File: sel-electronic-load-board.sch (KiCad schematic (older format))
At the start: 44 parts, among them J1 HE10 receptacle, Q1 N-mosfet, Q10 N-mosfet, Q11 N-mosfet, Q12 N-mosfet, Q13 N-mosfet, Q14 N-mosfet, Q15 N-mosfet, Q16 N-mosfet, Q2 N-mosfet, Q3 N-mosfet, Q4 N-mosfet, Q5 N-mosfet, Q6 N-mosfet, Q7 N-mosfet, Q8 N-mosfet, Q9 N-mosfet, SW1 DMM bypass, U1 OpAmp, U2 Input stage, U3 Output stage, U4 Current sensor

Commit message: assigning footprint, missing lever switch
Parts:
- F1: footprint (none) -> Fuse:Fuseholder_Cylinder-5x20mm_Stelvio-Kontek_PTF78_Horizontal_Open
- H1, H2, H3, H4: footprint (none) -> MountingHole:MountingHole_4.3mm_M4_Pad
- H5, H6, H7, H8: footprint (none) -> MountingHole:MountingHole_4.3mm_M4
- J1: footprint (none) -> Connector_IDC:IDC-Header_2x05_P2.54mm_Horizontal
- JP1: footprint (none) -> Jumper:SolderJumper-2_P1.3mm_Open_RoundedPad1.0x1.5mm
- Q1, Q10, Q11, Q12, Q13, Q14, Q15, Q16, Q2, Q3, Q4, Q5, Q6, Q7, Q8, Q9: footprint electronic-load:TO220-GDS-Heatsink-1000mils-interaxe-91mils-pin-radius -> Package_TO_SOT_THT:TO-220-3_Vertical
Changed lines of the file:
@@
 F 0 "Q1" H 1400 1550 50  0000 L CNN
 F 1 "N-mosfet" H 1400 1450 50  0000 L CNN
-F 2 "electronic-load:TO220-GDS-Heatsink-1000mils-interaxe-91mils-pin-radius" H 1400 1600 50  0001 C CNN
+F 2 "Package_TO_SOT_THT:TO-220-3_Vertical" H 1400 1600 50  0001 C CNN
 F 3 "~" H 1200 1500 50  0001 C CNN
 	1    1200 1500
@@
 F 0 "Q2" H 2600 1550 50  0000 L CNN
 F 1 "N-mosfet" H 2600 1450 50  0000 L CNN
-F 2 "electronic-load:TO220-GDS-Heatsink-1000mils-interaxe-91mils-pin-radius" H 2600 1600 50  0001 C CNN
+F 2 "Package_TO_SOT_THT:TO-220-3_Vertical" H 2600 1600 50  0001 C CNN
 F 3 "~" H 2400 1500 50  0001 C CNN
 	1    2400 1500
@@
 F 0 "Q3" H 3800 1550 50  0000 L CNN
 F 1 "N-mosfet" H 3800 1450 50  0000 L CNN
-F 2 "electronic-load:TO220-GDS-Heatsink-1000mils-interaxe-91mils-pin-radius" H 3800 1600 50  0001 C CNN
+F 2 "Package_TO_SOT_THT:TO-220-3_Vertical" H 3800 1600 50  0001 C CNN
 F 3 "~" H 3600 1500 50  0001 C CNN
 	1    3600 1500
@@
 F 0 "Q4" H 5000 1550 50  0000 L CNN
 F 1 "N-mosfet" H 5000 1450 50  0000 L CNN
-F 2 "electronic-load:TO220-GDS-Heatsink-1000mils-interaxe-91mils-pin-radius" H 5000 1600 50  0001 C CNN
+F 2 "Package_TO_SOT_THT:TO-220-3_Vertical" H 5000 1600 50  0001 C CNN
 F 3 "~" H 4800 1500 50  0001 C CNN
 	1    4800 1500
@@
 F 0 "Q5" H 1400 2550 50  0000 L CNN
 F 1 "N-mosfet" H 1400 2450 50  0000 L CNN
-F 2 "electronic-load:TO220-GDS-Heatsink-1000mils-interaxe-91mils-pin-radius" H 1400 2600 50  0001 C CNN
+F 2 "Package_TO_SOT_THT:TO-220-3_Vertical" H 1400 2600 50  0001 C CNN
 F 3 "~" H 1200 2500 50  0001 C CNN
 	1    1200 2500
@@
 F 0 "Q6" H 2600 2550 50  0000 L CNN
 F 1 "N-mosfet" H 2600 2450 50  0000 L CNN
-F 2 "electronic-load:TO220-GDS-Heatsink-1000mils-interaxe-91mils-pin-radius" H 2600 2600 50  0001 C CNN
+F 2 "Package_TO_SOT_THT:TO-220-3_Vertical" H 2600 2600 50  0001 C CNN
 F 3 "~" H 2400 2500 50  0001 C CNN
 	1    2400 2500
@@
 F 0 "Q7" H 3800 2550 50  0000 L CNN
 F 1 "N-mosfet" H 3800 2450 50  0000 L CNN
-F 2 "electronic-load:TO220-GDS-Heatsink-1000mils-interaxe-91mils-pin-radius" H 3800 2600 50  0001 C CNN
+F 2 "Package_TO_SOT_THT:TO-220-3_Vertical" H 3800 2600 50  0001 C CNN
 F 3 "~" H 3600 2500 50  0001 C CNN
 	1    3600 2500
@@
 F 0 "Q8" H 5000 2550 50  0000 L CNN
 F 1 "N-mosfet" H 5000 2450 50  0000 L CNN
-F 2 "electronic-load:TO220-GDS-Heatsink-1000mils-interaxe-91mils-pin-radius" H 5000 2600 50  0001 C CNN
+F 2 "Package_TO_SOT_THT:TO-220-3_Vertical" H 5000 2600 50  0001 C CNN
 F 3 "~" H 4800 2500 50  0001 C CNN
 	1    4800 2500
@@
 F 0 "Q9" H 1400 3550 50  0000 L CNN
 F 1 "N-mosfet" H 1400 3450 50  0000 L CNN
-F 2 "electronic-load:TO220-GDS-Heatsink-1000mils-interaxe-91mils-pin-radius" H 1400 3600 50  0001 C CNN
+F 2 "Package_TO_SOT_THT:TO-220-3_Vertical" H 1400 3600 50  0001 C CNN
 F 3 "~" H 1200 3500 50  0001 C CNN
 	1    1200 3500
@@
 F 0 "Q10" H 2600 3550 50  0000 L CNN
 F 1 "N-mosfet" H 2600 3450 50  0000 L CNN
-F 2 "electronic-load:TO220-GDS-Heatsink-1000mils-interaxe-91mils-pin-radius" H 2600 3600 50  0001 C CNN
+F 2 "Package_TO_SOT_THT:TO-220-3_Vertical" H 2600 3600 50  0001 C CNN
 F 3 "~" H 2400 3500 50  0001 C CNN
 	1    2400 3500
@@
 F 0 "Q11" H 3800 3550 50  0000 L CNN
 F 1 "N-mosfet" H 3800 3450 50  0000 L CNN
-F 2 "electronic-load:TO220-GDS-Heatsink-1000mils-interaxe-91mils-pin-radius" H 3800 3600 50  0001 C CNN
+F 2 "Package_TO_SOT_THT:TO-220-3_Vertical" H 3800 3600 50  0001 C CNN
 F 3 "~" H 3600 3500 50  0001 C CNN
 	1    3600 3500
@@
 F 0 "Q12" H 5000 3550 50  0000 L CNN
 F 1 "N-mosfet" H 5000 3450 50  0000 L CNN
-F 2 "electronic-load:TO220-GDS-Heatsink-1000mils-interaxe-91mils-pin-radius" H 5000 3600 50  0001 C CNN
+F 2 "Package_TO_SOT_THT:TO-220-3_Vertical" H 5000 3600 50  0001 C CNN
 F 3 "~" H 4800 3500 50  0001 C CNN
 	1    4800 3500
@@
 F 0 "Q13" H 1400 4550 50  0000 L CNN
 F 1 "N-mosfet" H 1400 4450 50  0000 L CNN
-F 2 "electronic-load:TO220-GDS-Heatsink-1000mils-interaxe-91mils-pin-radius" H 1400 4600 50  0001 C CNN
+F 2 "Package_TO_SOT_THT:TO-220-3_Vertical" H 1400 4600 50  0001 C CNN
 F 3 "~" H 1200 4500 50  0001 C CNN
 	1    1200 4500
@@
 F 0 "Q14" H 2600 4550 50  0000 L CNN
 F 1 "N-mosfet" H 2600 4450 50  0000 L CNN
-F 2 "electronic-load:TO220-GDS-Heatsink-1000mils-interaxe-91mils-pin-radius" H 2600 4600 50  0001 C CNN
+F 2 "Package_TO_SOT_THT:TO-220-3_Vertical" H 2600 4600 50  0001 C CNN
 F 3 "~" H 2400 4500 50  0001 C CNN
 	1    2400 4500
@@
 F 0 "Q15" H 3800 4550 50  0000 L CNN
 F 1 "N-mosfet" H 3800 4450 50  0000 L CNN
-F 2 "electronic-load:TO220-GDS-Heatsink-1000mils-interaxe-91mils-pin-radius" H 3800 4600 50  0001 C CNN
+F 2 "Package_TO_SOT_THT:TO-220-3_Vertical" H 3800 4600 50  0001 C CNN
 F 3 "~" H 3600 4500 50  0001 C CNN
 	1    3600 4500
@@
 F 0 "Q16" H 5000 4550 50  0000 L CNN
 F 1 "N-mosfet" H 5000 4450 50  0000 L CNN
-F 2 "electronic-load:TO220-GDS-Heatsink-1000mils-interaxe-91mils-pin-radius" H 5000 4600 50  0001 C CNN
+F 2 "Package_TO_SOT_THT:TO-220-3_Vertical" H 5000 4600 50  0001 C CNN
 F 3 "~" H 4800 4500 50  0001 C CNN
 	1    4800 4500
@@
 F 0 "H2" H 3100 6350 50  0000 C CNN
 F 1 "DUT-" H 3100 6275 50  0000 C CNN
-F 2 "" H 3100 6100 50  0001 C CNN
+F 2 "MountingHole:MountingHole_4.3mm_M4_Pad" H 3100 6100 50  0001 C CNN
 F 3 "~" H 3100 6100 50  0001 C CNN
 	1    3100 6100
@@
 F 0 "H4" H 3850 6350 50  0000 C CNN
 F 1 "DMM-" H 3850 6275 50  0000 C CNN
-F 2 "" H 3850 6100 50  0001 C CNN
+F 2 "MountingHole:MountingHole_4.3mm_M4_Pad" H 3850 6100 50  0001 C CNN
 F 3 "~" H 3850 6100 50  0001 C CNN
 	1    3850 6100
@@
 F 0 "H3" H 3600 6350 50  0000 C CNN
 F 1 "DMM+" H 3600 6275 50  0000 C CNN
-F 2 "" H 3600 6100 50  0001 C CNN
+F 2 "MountingHole:MountingHole_4.3mm_M4_Pad" H 3600 6100 50  0001 C CNN
 F 3 "~" H 3600 6100 50  0001 C CNN
 	1    3600 6100
@@
 F 0 "H1" H 2850 6350 50  0000 C CNN
 F 1 "DUT+" H 2850 6275 50  0000 C CNN
-F 2 "" H 2850 6100 50  0001 C CNN
+F 2 "MountingHole:MountingHole_4.3mm_M4_Pad" H 2850 6100 50  0001 C CNN
 F 3 "~" H 2850 6100 50  0001 C CNN
 	1    2850 6100
@@
 F 0 "F1" V 3430 6500 50  0000 C CNN
 F 1 "Fuse 4A" V 3275 6500 50  0000 C CNN
-F 2 "" V 3280 6500 50  0001 C CNN
+F 2 "Fuse:Fuseholder_Cylinder-5x20mm_Stelvio-Kontek_PTF78_Horizontal_Open" V 3280 6500 50  0001 C CNN
 F 3 "~" H 3350 6500 50  0001 C CNN
 	1    3350 6500
@@
 F 0 "J1" H 1500 6600 50  0000 C CNN
 F 1 "HE10 receptacle" H 1500 6000 50  0000 C CNN
-F 2 "" H 1450 6300 50  0001 C CNN
+F 2 "Connector_IDC:IDC-Header_2x05_P2.54mm_Horizontal" H 1450 6300 50  0001 C CNN
 F 3 "~" H 1450 6300 50  0001 C CNN
 	1    1450 6300
@@
 F 0 "H5" H 6500 6700 50  0000 C CNN
 F 1 "MountingHole" H 6500 6625 50  0000 C CNN
-F 2 "" H 6500 6500 50  0001 C CNN
+F 2 "MountingHole:MountingHole_4.3mm_M4" H 6500 6500 50  0001 C CNN
 F 3 "~" H 6500 6500 50  0001 C CNN
 	1    6500 6500
@@
 F 0 "H6" H 6500 7050 50  0000 C CNN
 F 1 "MountingHole" H 6500 6975 50  0000 C CNN
-F 2 "" H 6500 6850 50  0001 C CNN
+F 2 "MountingHole:MountingHole_4.3mm_M4" H 6500 6850 50  0001 C CNN
 F 3 "~" H 6500 6850 50  0001 C CNN
 	1    6500 6850
@@
 F 0 "H7" H 6500 7400 50  0000 C CNN
 F 1 "MountingHole" H 6500 7325 50  0000 C CNN
-F 2 "" H 6500 7200 50  0001 C CNN
+F 2 "MountingHole:MountingHole_4.3mm_M4" H 6500 7200 50  0001 C CNN
 F 3 "~" H 6500 7200 50  0001 C CNN
 	1    6500 7200
@@
 F 0 "H8" H 6500 7750 50  0000 C CNN
 F 1 "MountingHole" H 6500 7675 50  0000 C CNN
-F 2 "" H 6500 7550 50  0001 C CNN
+F 2 "MountingHole:MountingHole_4.3mm_M4" H 6500 7550 50  0001 C CNN
 F 3 "~" H 6500 7550 50  0001 C CNN
 	1    6500 7550
@@
 F 0 "JP1" H 5250 7180 50  0000 C CNN
 F 1 "If needed by the IC" H 5250 6950 50  0000 C CNN
-F 2 "" H 5250 7100 50  0001 C CNN
+F 2 "Jumper:SolderJumper-2_P1.3mm_Open_RoundedPad1.0x1.5mm" H 5250 7100 50  0001 C CNN
 F 3 "~" H 5250 7100 50  0001 C CNN
 	1    5250 7100

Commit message: update metadata, use custom footprint for toggle switch
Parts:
- SW1: footprint (none) -> switches:toggle-switch-P4.70mm-3pins-75mils-vias
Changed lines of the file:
@@
 encoding utf-8
 Sheet 1 1
-Title ""
-Date "2022-05-13"
-Rev ""
+Title "Electronic load module"
+Date "2022-05-15"
+Rev "1.0.0-draft"
 Comp ""
 Comment1 ""
@@
 F 0 "SW1" H 3900 6300 50  0000 C CNN
 F 1 "DMM bypass" H 3900 6200 50  0000 C CNN
-F 2 "" H 3900 6500 50  0001 C CNN
+F 2 "switches:toggle-switch-P4.70mm-3pins-75mils-vias" H 3900 6500 50  0001 C CNN
 F 3 "~" H 3900 6500 50  0001 C CNN
 	1    3900 6500

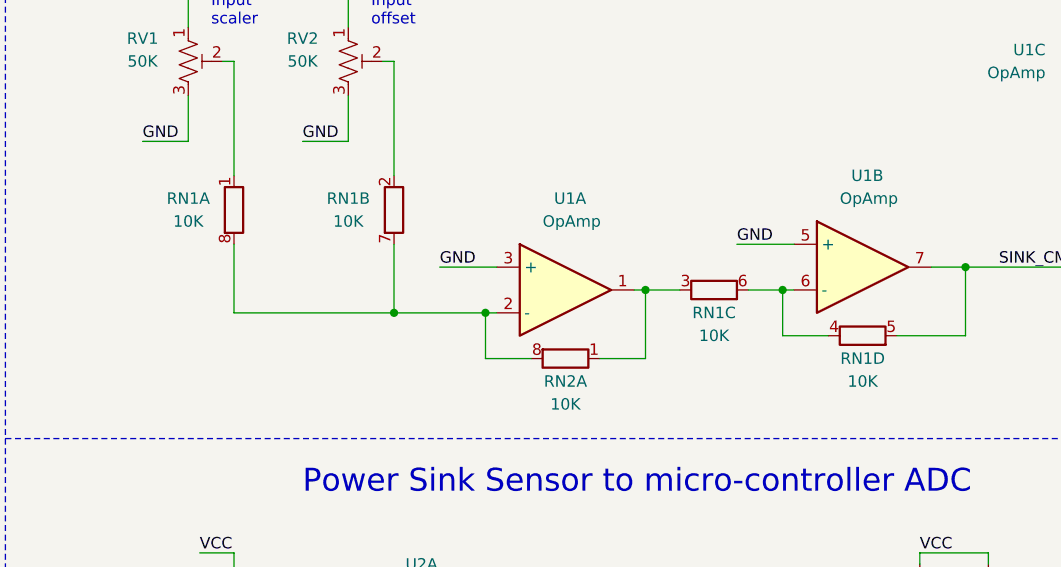
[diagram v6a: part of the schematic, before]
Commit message: reorganize copper pour, traces, DMM and bypass, connector to main board
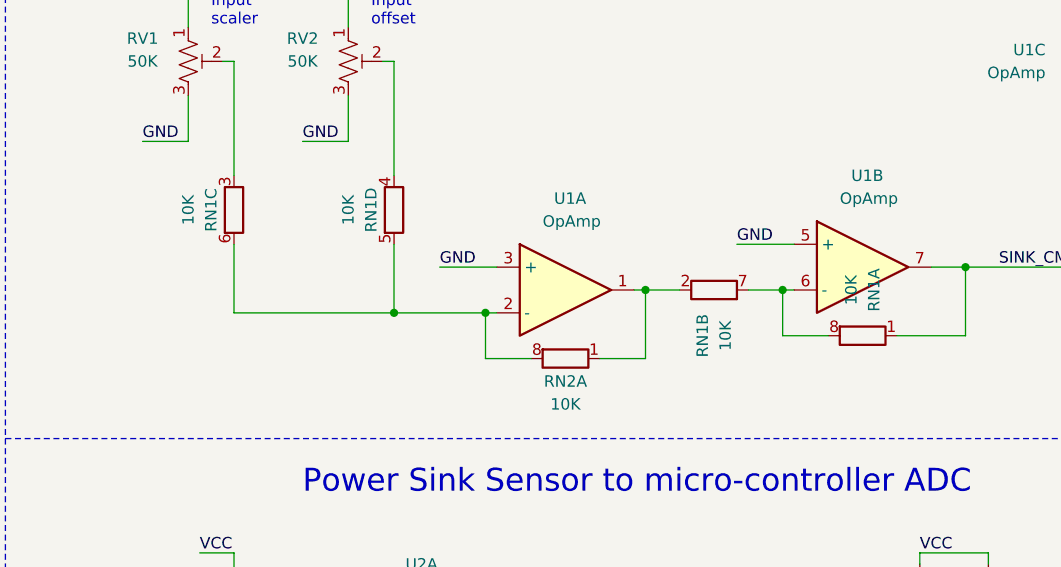
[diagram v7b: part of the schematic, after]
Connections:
- net SINK_CMD: now also RN1.1 (R1.1); no longer RN1.5 (R4.2)
- net at RN2.1 (R1.1), U1.1: now also RN1.2 (R2.1); no longer RN1.3 (R3.1)
- net at RN2.8 (R1.2), U1.2 (-): now also RN1.5 (R4.2), RN1.6 (R3.2); no longer RN1.7 (R2.2), RN1.8 (R1.2)
- net at RV1.2: now also RN1.3 (R3.1); no longer RN1.1 (R1.1)
- net at RV2.2: now also RN1.4 (R4.1); no longer RN1.2 (R2.1)
- new net: RN1.7 (R2.2), RN1.8 (R1.2), U1.6 (-)
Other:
- moved on the sheet: RN1A, RN1B, RN1C, RN1D
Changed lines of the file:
@@
 L Device:R_Pack04_Split RN?
 U 4 1 627FE4E1
-P 9250 2600
+P 7200 2050
 AR Path="/627E1114/617D6ABB/627FE4E1" Ref="RN?"  Part="2"
 AR Path="/627FE4E1" Ref="RN1"  Part="4"
-F 0 "RN1" V 9350 2600 50  0000 C CNN
-F 1 "10K" V 9450 2600 50  0000 C CNN
-F 2 "Resistor_SMD:R_Array_Convex_4x0603" V 9170 2600 50  0001 C CNN
-F 3 "http://www.vishay.com/docs/31509/csc.pdf" H 9250 2600 50  0001 C CNN
-	4    9250 2600
-	0    1    1    0
+F 0 "RN1" V 7300 2050 50  0000 C CNN
+F 1 "10K" V 7400 2050 50  0000 C CNN
+F 2 "Resistor_SMD:R_Array_Convex_4x0603" V 7120 2050 50  0001 C CNN
+F 3 "http://www.vishay.com/docs/31509/csc.pdf" H 7200 2050 50  0001 C CNN
+	4    7200 2050
+	-1   0    0    1
 $EndComp
 $Comp
 L Device:R_Pack04_Split RN?
 U 3 1 627FE4E7
-P 8600 2400
+P 6500 2050
 AR Path="/627E1114/617D6ABB/627FE4E7" Ref="RN?"  Part="1"
 AR Path="/627FE4E7" Ref="RN1"  Part="3"
-F 0 "RN1" V 8700 2400 50  0000 C CNN
-F 1 "10K" V 8800 2400 50  0000 C CNN
-F 2 "Resistor_SMD:R_Array_Convex_4x0603" V 8520 2400 50  0001 C CNN
-F 3 "http://www.vishay.com/docs/31509/csc.pdf" H 8600 2400 50  0001 C CNN
-	3    8600 2400
-	0    1    1    0
+F 0 "RN1" V 6600 2050 50  0000 C CNN
+F 1 "10K" V 6700 2050 50  0000 C CNN
+F 2 "Resistor_SMD:R_Array_Convex_4x0603" V 6420 2050 50  0001 C CNN
+F 3 "http://www.vishay.com/docs/31509/csc.pdf" H 6500 2050 50  0001 C CNN
+	3    6500 2050
+	-1   0    0    1
 $EndComp
 $Comp
@@
 L Device:R_Pack04_Split RN?
 U 2 1 627FE4F3
-P 7200 2050
+P 8600 2400
 AR Path="/627E1114/617D6ABB/627FE4F3" Ref="RN?"  Part="2"
 AR Path="/627FE4F3" Ref="RN1"  Part="2"
-F 0 "RN1" H 7400 2000 50  0000 C CNN
-F 1 "10K" H 7400 2100 50  0000 C CNN
-F 2 "Resistor_SMD:R_Array_Convex_4x0603" V 7120 2050 50  0001 C CNN
-F 3 "http://www.vishay.com/docs/31509/csc.pdf" H 7200 2050 50  0001 C CNN
-	2    7200 2050
-	-1   0    0    1
+F 0 "RN1" H 8800 2350 50  0000 C CNN
+F 1 "10K" H 8800 2450 50  0000 C CNN
+F 2 "Resistor_SMD:R_Array_Convex_4x0603" V 8520 2400 50  0001 C CNN
+F 3 "http://www.vishay.com/docs/31509/csc.pdf" H 8600 2400 50  0001 C CNN
+	2    8600 2400
+	0    1    1    0
 $EndComp
 $Comp
 L Device:R_Pack04_Split RN?
 U 1 1 627FE4F9
-P 6500 2050
+P 9250 2600
 AR Path="/627E1114/617D6ABB/627FE4F9" Ref="RN?"  Part="1"
 AR Path="/627FE4F9" Ref="RN1"  Part="1"
-F 0 "RN1" H 6700 2000 50  0000 C CNN
-F 1 "10K" H 6700 2100 50  0000 C CNN
-F 2 "Resistor_SMD:R_Array_Convex_4x0603" V 6420 2050 50  0001 C CNN
-F 3 "http://www.vishay.com/docs/31509/csc.pdf" H 6500 2050 50  0001 C CNN
-	1    6500 2050
-	-1   0    0    1
+F 0 "RN1" H 9450 2550 50  0000 C CNN
+F 1 "10K" H 9450 2650 50  0000 C CNN
+F 2 "Resistor_SMD:R_Array_Convex_4x0603" V 9170 2600 50  0001 C CNN
+F 3 "http://www.vishay.com/docs/31509/csc.pdf" H 9250 2600 50  0001 C CNN
+	1    9250 2600
+	0    -1   -1   0
 $EndComp
 Wire Wire Line

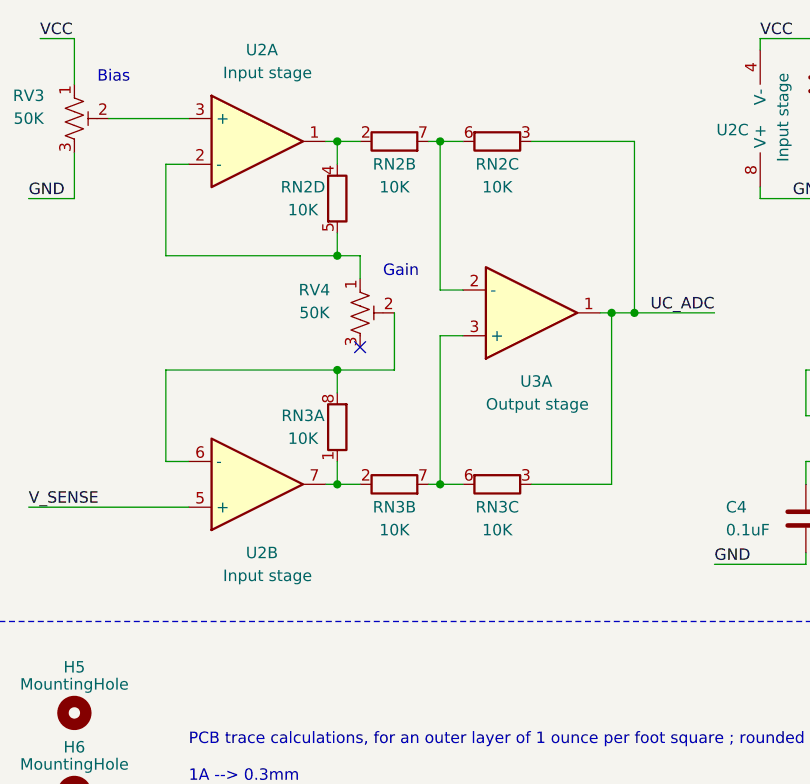
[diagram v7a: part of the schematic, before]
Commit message: done tracing, optimizing the use of network resistors units
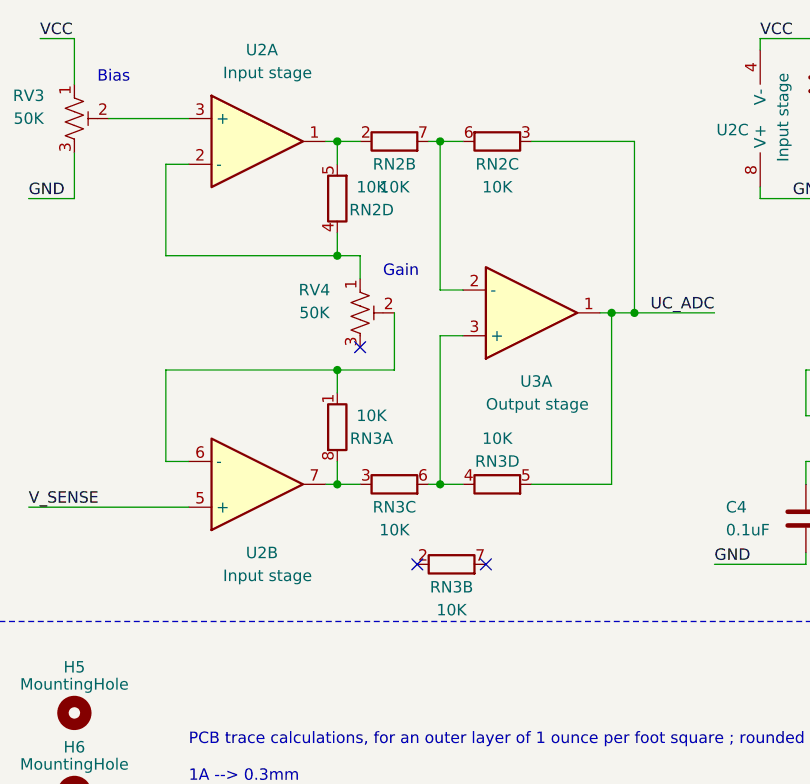
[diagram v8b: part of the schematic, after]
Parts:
- added unit 2 of RN3
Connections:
- net UC_ADC: now also RN3.5 (R4.2); no longer RN3.3 (R3.1)
- net at RN2.2 (R2.1), U2.1: now also RN2.5 (R4.2); no longer RN2.4 (R4.1)
- net at RV4.1, U2.2 (-): now also RN2.4 (R4.1); no longer RN2.5 (R4.2)
- net at RV4.2, U2.6 (-): now also RN3.1 (R1.1); no longer RN3.8 (R1.2)
- new net: RN3.3 (R3.1), RN3.8 (R1.2), U2.7
- new net: RN3.4 (R4.1), RN3.6 (R3.2), U3.3 (+)
- no-connect marks 2 -> 4
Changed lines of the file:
@@
 $Comp
 L Device:R_Pack04_Split RN?
-U 2 1 62867A5A
+U 3 1 62867A5A
 P 7900 5500
 AR Path="/627E1114/617D5FF5/62867A5A" Ref="RN?"  Part="1"
-AR Path="/62867A5A" Ref="RN3"  Part="2"
+AR Path="/62867A5A" Ref="RN3"  Part="3"
 F 0 "RN3" V 8000 5500 50  0000 C CNN
 F 1 "10K" V 8100 5500 50  0000 C CNN
 F 2 "Resistor_SMD:R_Array_Convex_4x0603" V 7820 5500 50  0001 C CNN
 F 3 "http://www.vishay.com/docs/31509/csc.pdf" H 7900 5500 50  0001 C CNN
-	2    7900 5500
+	3    7900 5500
 	0    1    1    0
 $EndComp
@@
 $Comp
 L Device:R_Pack04_Split RN?
-U 3 1 62867A8F
+U 4 1 62867A8F
 P 8350 5500
 AR Path="/627E1114/617D5FF5/62867A8F" Ref="RN?"  Part="4"
-AR Path="/62867A8F" Ref="RN3"  Part="3"
+AR Path="/62867A8F" Ref="RN3"  Part="4"
 F 0 "RN3" V 8250 5500 50  0000 C CNN
 F 1 "10K" V 8150 5500 50  0000 C CNN
 F 2 "Resistor_SMD:R_Array_Convex_4x0603" V 8270 5500 50  0001 C CNN
 F 3 "http://www.vishay.com/docs/31509/csc.pdf" H 8350 5500 50  0001 C CNN
-	3    8350 5500
-	0    -1   -1   0
+	4    8350 5500
+	0    1    1    0
 $EndComp
 $Comp
@@
 F 3 "http://www.vishay.com/docs/31509/csc.pdf" H 7650 4250 50  0001 C CNN
 	4    7650 4250
-	-1   0    0    1
+	1    0    0    -1
 $EndComp
 $Comp
@@
 F 3 "http://www.vishay.com/docs/31509/csc.pdf" H 7650 5250 50  0001 C CNN
 	1    7650 5250
-	1    0    0    -1
+	-1   0    0    1
 $EndComp
 Wire Wire Line
@@
 Wire Wire Line
 	9500 3550 9500 3600
+$Comp
+L Device:R_Pack04_Split RN?
+U 2 1 62885B53
+P 8150 5850
+AR Path="/627E1114/617D5FF5/62885B53" Ref="RN?"  Part="1"
+AR Path="/62885B53" Ref="RN3"  Part="2"
+F 0 "RN3" V 8250 5850 50  0000 C CNN
+F 1 "10K" V 8350 5850 50  0000 C CNN
+F 2 "Resistor_SMD:R_Array_Convex_4x0603" V 8070 5850 50  0001 C CNN
+F 3 "http://www.vishay.com/docs/31509/csc.pdf" H 8150 5850 50  0001 C CNN
+	2    8150 5850
+	0    1    1    0
+$EndComp
+NoConn ~ 8000 5850
+NoConn ~ 8300 5850
 $EndSCHEMATC
